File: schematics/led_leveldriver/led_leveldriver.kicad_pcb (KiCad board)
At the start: 2 copper layers, 22 parts, among them IC1 TPIC6B595, J1 Conn_02x04_Odd_Even, Q1 Q_PMOS_GSD, Q2 Q_PMOS_GSD, Q3 Q_PMOS_GSD, Q4 Q_PMOS_GSD, Q5 Q_PMOS_GSD, Q6 Q_PMOS_GSD, Q7 Q_PMOS_GSD, Q8 Q_PMOS_GSD

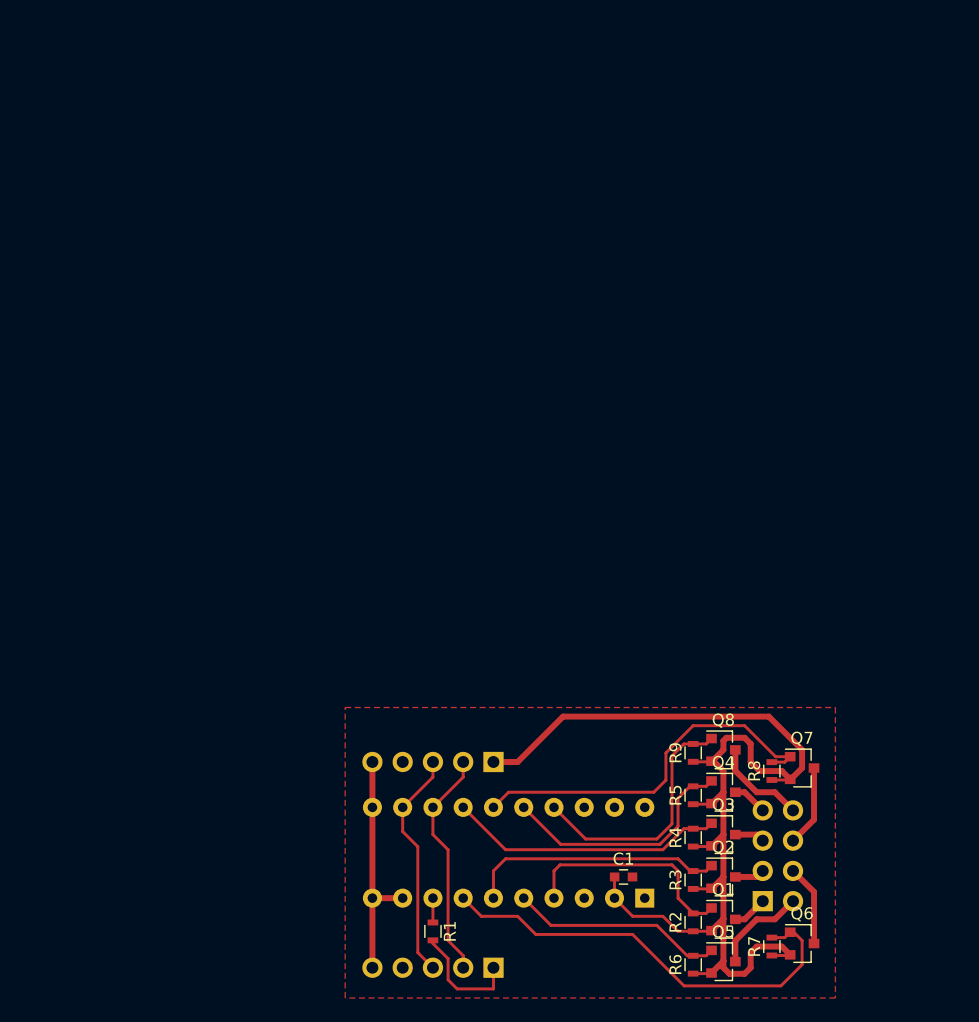
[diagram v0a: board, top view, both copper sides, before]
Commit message: Rework Level driver to STM32 breakout board
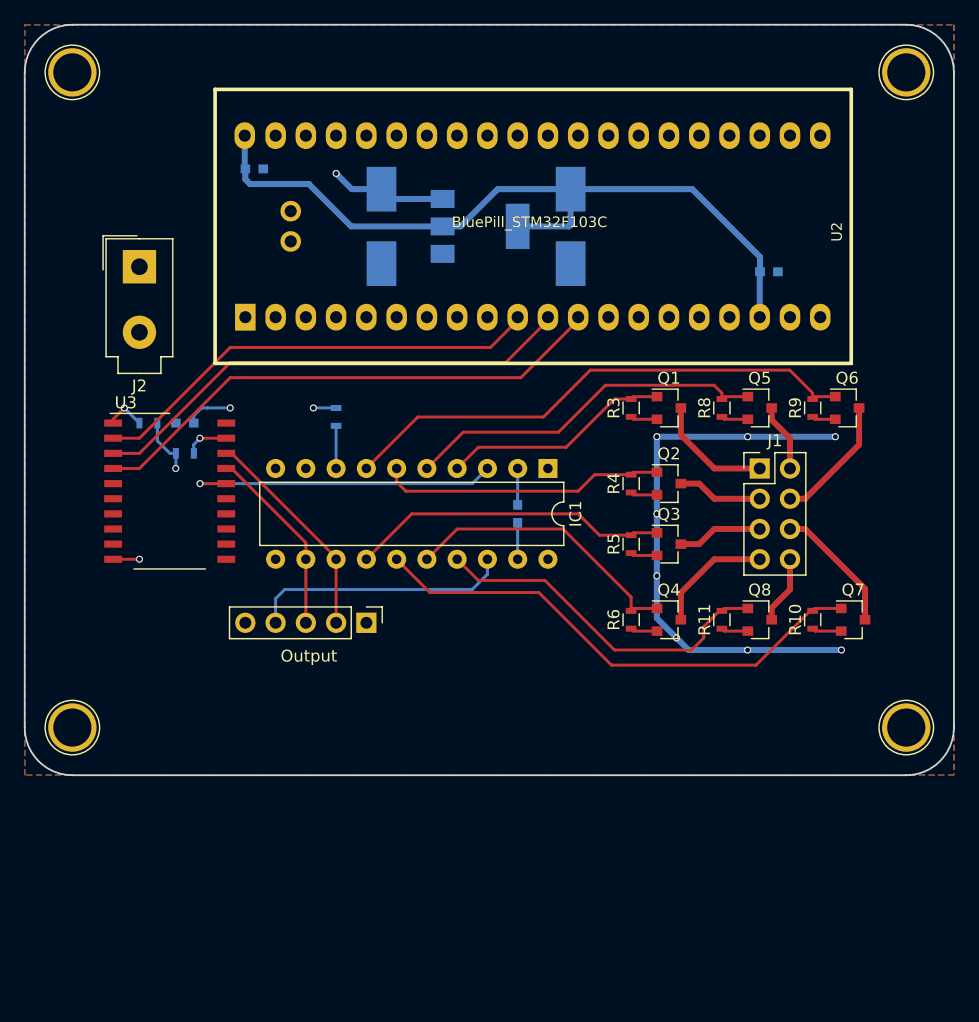
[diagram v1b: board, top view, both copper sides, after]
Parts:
- removed BOARD_IN1, BOARD_OUT1: CONN_01X05, Pin_Headers:Pin_Header_Straight_1x05_Pitch2.54mm
- added C2: 10u, Capacitors_Tantalum_SMD:CP_Tantalum_Case-U_EIA-6032-15_Hand, B.Cu at (153.6, 51.8)
- added C3: 0.1uF, Capacitors_SMD:C_0603, B.Cu at (170.2, 55.6)
- added C4: 0.1uF, Capacitors_SMD:C_0603, B.Cu at (121.2, 68.3)
- added C5: 0.1uF, Capacitors_SMD:C_0603, B.Cu at (149.1, 75.9)
- added C6: 0.1uF, Capacitors_SMD:C_0603, B.Cu at (127.0, 46.9)
- added J2: 5V_IN, Connectors_Molex:Molex_MiniFit-JR-5556-02A_2x01x4.20mm_Straight, F.Cu at (117.4, 55.1)
- added Output: CONN_01X05, Pin_Headers:Pin_Header_Straight_1x05_Pitch2.54mm, F.Cu at (136.4, 85.0)
- added R10: 10k, Resistors_SMD:R_0603, F.Cu at (173.9, 84.8)
- added R11: 10k, Resistors_SMD:R_0603, F.Cu at (166.3, 84.8)
- added REF**: 1pin, Connect:1pin, F.Cu at (181.7, 93.8)
- added REF**: 1pin, Connect:1pin, F.Cu at (111.7, 93.8)
- added REF**: 1pin, Connect:1pin, F.Cu at (181.7, 38.8)
- added REF**: 1pin, Connect:1pin, F.Cu at (111.7, 38.8)
- added U1: LM1117-3.3, TO_SOT_Packages_SMD:SOT-223-3_TabPin2, B.Cu at (146.0, 51.8)
- added U2: BluePill_STM32F103C, BluePill_breakouts:BluePill_STM32F103C, F.Cu at (126.3, 59.4)
- added U3: 74HCT245, Housings_SOIC:SO-20_12.8x7.5mm_Pitch1.27mm, F.Cu at (119.9, 74.0)
- C1: value 0.1uF -> 10u; footprint Capacitors_SMD:C_0603 -> Capacitors_Tantalum_SMD:CP_Tantalum_Case-U_EIA-6032-15_Hand; moved to B.Cu
- IC1: moved to F.Cu
- J1: footprint Pin_Headers:Pin_Header_Angled_2x04_Pitch2.54mm -> Pin_Headers:Pin_Header_Straight_2x04_Pitch2.54mm; moved to F.Cu
- R1, R2, R7: moved to B.Cu
- moved R2 62.0 mm to (118.1, 68.3), turned to 180 degrees
- moved C1 58.3 mm to (137.7, 51.8), turned to 270 degrees
- moved R7 57.6 mm to (133.9, 67.7)
- moved Q5 46.6 mm to (169.4, 67.0)
- moved R1 45.2 mm to (121.2, 70.8), turned to 0 degrees
- moved Q6 45.1 mm to (176.8, 67.0)
- moved Q1 43.2 mm to (161.8, 67.0)
- moved R3 40.0 mm to (158.6, 67.0)
- moved IC1 37.0 mm to (151.7, 72.1), turned to 270 degrees
- moved J1 36.3 mm to (169.4, 72.1)
- moved Q2 33.3 mm to (161.8, 73.3)
- moved R8 30.8 mm to (166.3, 67.0)
- moved R9 30.6 mm to (173.9, 67.0)
- moved R4 30.2 mm to (158.6, 73.3)
- moved R6 29.4 mm to (158.6, 84.8)
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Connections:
- IC1 pad 14: Net-(IC1-Pad14) -> /L4
- IC1 pad 15: Net-(IC1-Pad15) -> /L5
- IC1 pad 16: Net-(IC1-Pad16) -> /L6
- IC1 pad 17: Net-(IC1-Pad17) -> /L7
- IC1 pad 18: Net-(BOARD_OUT1-Pad4) -> /DOUT
- IC1 pad 3: Net-(BOARD_IN1-Pad4) -> /DATA
- IC1 pad 4: Net-(IC1-Pad4) -> /L0
- IC1 pad 5: Net-(IC1-Pad5) -> /L1
- IC1 pad 6: Net-(IC1-Pad6) -> /L2
- IC1 pad 7: Net-(IC1-Pad7) -> /L3
- Q1 pad 1: Net-(IC1-Pad4) -> /L0
- Q2 pad 1: Net-(IC1-Pad6) -> /L2
- Q3 pad 1: Net-(IC1-Pad14) -> /L4
- Q4 pad 1: Net-(IC1-Pad16) -> /L6
- Q5 pad 1: Net-(IC1-Pad5) -> /L1
- Q6 pad 1: Net-(IC1-Pad7) -> /L3
- Q7 pad 1: Net-(IC1-Pad15) -> /L5
- Q8 pad 1: Net-(IC1-Pad17) -> /L7
- R1 pad 1: Net-(IC1-Pad8) -> VCC
- R1 pad 2: VCC -> Net-(R1-Pad2)
- R2 pad 2: Net-(IC1-Pad4) -> Net-(R2-Pad2)
- R3 pad 2: Net-(IC1-Pad6) -> /L0
- R4 pad 2: Net-(IC1-Pad14) -> /L2
- R5 pad 2: Net-(IC1-Pad16) -> /L4
- R6 pad 2: Net-(IC1-Pad5) -> /L6
- R7 pad 1: VCC -> Net-(IC1-Pad8)
- R7 pad 2: Net-(IC1-Pad7) -> VCC
- R8 pad 2: Net-(IC1-Pad15) -> /L1
- R9 pad 2: Net-(IC1-Pad17) -> /L3
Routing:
- net +3V3: track 0.00 -> 64.7 mm
- net Net-(U2-Pad12): track 0.00 -> 44.7 mm
- net /L3: track 0.00 -> 44.2 mm
- net /L5: track 0.00 -> 43.0 mm
- net Net-(U2-Pad11): track 0.00 -> 41.9 mm
- net Net-(U2-Pad10): track 0.00 -> 38.3 mm
- net Net-(IC1-Pad7): track 37.3 -> 0.00 mm
- net Net-(IC1-Pad15): track 31.9 -> 0.00 mm
- net /L1: track 0.00 -> 30.7 mm
- net /L7: track 0.00 -> 29.6 mm
- net /DATA: track 0.00 -> 26.9 mm, vias 0 -> 1
- net /L4: track 0.00 -> 26.8 mm
- net /L6: track 0.00 -> 24.0 mm
- net /L2: track 0.00 -> 24.0 mm
- net Net-(IC1-Pad14): track 23.2 -> 0.00 mm
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- added copper zone on B.Cu, net GND
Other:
- board outline added: 78 x 63 mm
